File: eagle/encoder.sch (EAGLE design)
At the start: 19 parts, among them IC1 LM339D, J1 SPI, U1 MCP42XXX, U2 ATMEGA328P

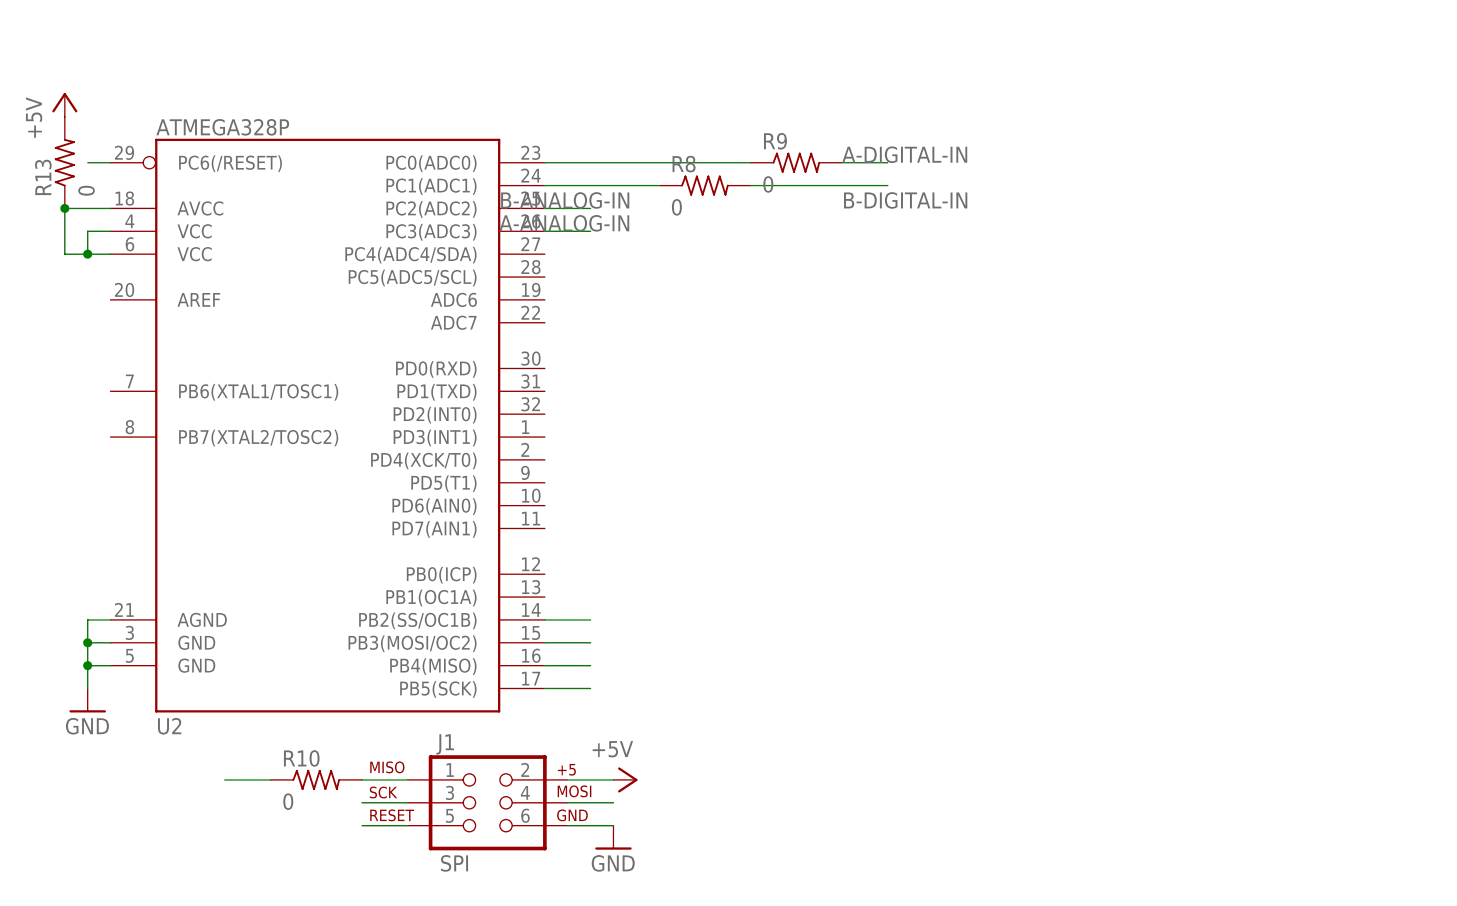
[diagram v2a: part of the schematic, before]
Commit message: Added crystal.
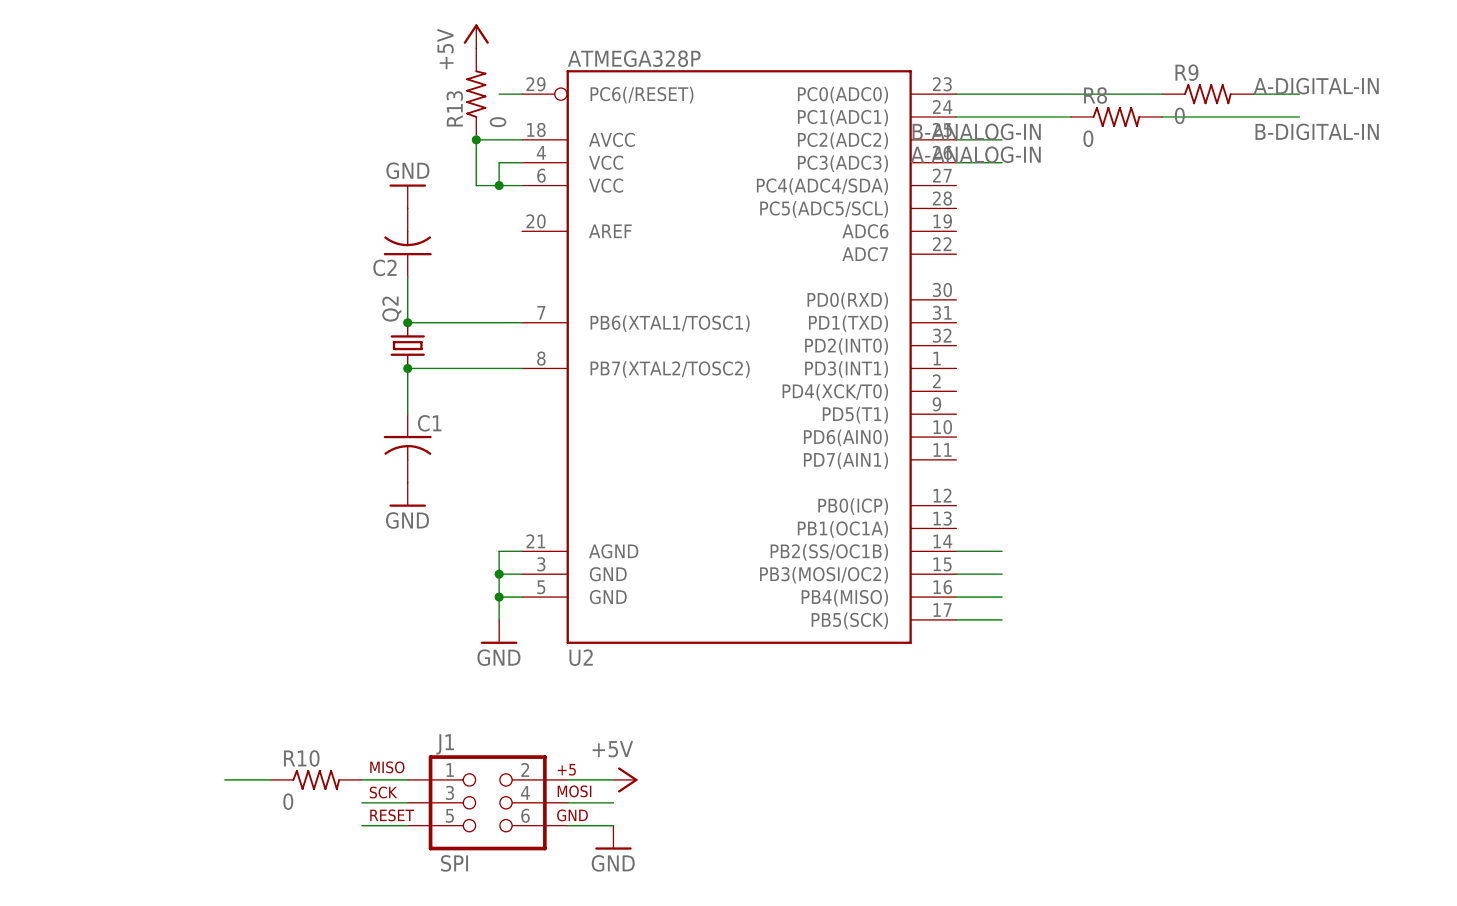
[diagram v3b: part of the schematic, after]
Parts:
- added C1, C2: (no value), resistor:C-USC1206
- added Q2: (no value), crystal:CRYSTALHC49UP
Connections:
- new net N$10: C1.1, Q2.1, U2.PB7(XTAL2/TOSC2)
- new net N$11: C2.1, Q2.2, U2.PB6(XTAL1/TOSC1)
- net GND: now also C1.2, C2.2
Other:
- moved on the sheet: R13, R8, R9, U2
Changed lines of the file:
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@@
 <part name="R13" library="resistor" deviceset="R-US_" device="R1206" value="0"/>
 <part name="P+12" library="supply1" deviceset="+5V" device=""/>
+<part name="Q2" library="crystal" deviceset="CRYSTAL" device="HC49UP"/>
+<part name="C1" library="resistor" deviceset="C-US" device="C1206"/>
+<part name="C2" library="resistor" deviceset="C-US" device="C1206"/>
+<part name="GND9" library="supply1" deviceset="GND" device=""/>
+<part name="GND10" library="supply1" deviceset="GND" device=""/>
 </parts>
 <sheets>
@@
 <instance part="R6" gate="G$1" x="66.04" y="111.76"/>
 <instance part="R7" gate="G$1" x="78.74" y="55.88"/>
-<instance part="U2" gate="G$1" x="25.4" y="177.8"/>
-<instance part="R8" gate="G$1" x="68.58" y="200.66"/>
-<instance part="R9" gate="G$1" x="78.74" y="203.2"/>
+<instance part="U2" gate="G$1" x="71.12" y="185.42"/>
+<instance part="R8" gate="G$1" x="114.3" y="208.28"/>
+<instance part="R9" gate="G$1" x="124.46" y="210.82"/>
 <instance part="R10" gate="G$1" x="25.4" y="134.62"/>
 <instance part="J1" gate="G$1" x="43.18" y="132.08"/>
 <instance part="P+11" gate="1" x="60.96" y="134.62" rot="R270"/>
 <instance part="GND8" gate="1" x="58.42" y="127"/>
-<instance part="GND6" gate="1" x="0" y="142.24"/>
+<instance part="GND6" gate="1" x="45.72" y="149.86"/>
 <instance part="R11" gate="G$1" x="60.96" y="35.56" rot="R90"/>
 <instance part="P+10" gate="1" x="60.96" y="43.18"/>
 <instance part="R12" gate="G$1" x="71.12" y="30.48" rot="R90"/>
-<instance part="R13" gate="G$1" x="-2.54" y="203.2" rot="R90"/>
-<instance part="P+12" gate="1" x="-2.54" y="210.82"/>
+<instance part="R13" gate="G$1" x="43.18" y="210.82" rot="R90"/>
+<instance part="P+12" gate="1" x="43.18" y="218.44"/>
+<instance part="Q2" gate="G$1" x="35.56" y="182.88" rot="R90"/>
+<instance part="C1" gate="G$1" x="35.56" y="172.72"/>
+<instance part="C2" gate="G$1" x="35.56" y="193.04" rot="R180"/>
+<instance part="GND9" gate="1" x="35.56" y="165.1"/>
+<instance part="GND10" gate="1" x="35.56" y="200.66" rot="R180"/>
 </instances>
 <busses>
@@
 <segment>
 <pinref part="U2" gate="G$1" pin="AGND"/>
-<wire x1="2.54" y1="152.4" x2="0" y2="152.4" width="0.1524" layer="91"/>
-<wire x1="0" y1="152.4" x2="0" y2="149.86" width="0.1524" layer="91"/>
+<wire x1="48.26" y1="160.02" x2="45.72" y2="160.02" width="0.1524" layer="91"/>
+<wire x1="45.72" y1="160.02" x2="45.72" y2="157.48" width="0.1524" layer="91"/>
 <pinref part="U2" gate="G$1" pin="GND@1"/>
-<wire x1="0" y1="149.86" x2="0" y2="147.32" width="0.1524" layer="91"/>
-<wire x1="0" y1="147.32" x2="0" y2="144.78" width="0.1524" layer="91"/>
-<wire x1="2.54" y1="149.86" x2="0" y2="149.86" width="0.1524" layer="91"/>
+<wire x1="45.72" y1="157.48" x2="45.72" y2="154.94" width="0.1524" layer="91"/>
+<wire x1="45.72" y1="154.94" x2="45.72" y2="152.4" width="0.1524" layer="91"/>
+<wire x1="48.26" y1="157.48" x2="45.72" y2="157.48" width="0.1524" layer="91"/>
 <pinref part="U2" gate="G$1" pin="GND@2"/>
-<wire x1="2.54" y1="147.32" x2="0" y2="147.32" width="0.1524" layer="91"/>
+<wire x1="48.26" y1="154.94" x2="45.72" y2="154.94" width="0.1524" layer="91"/>
 <pinref part="GND6" gate="1" pin="GND"/>
-<junction x="0" y="149.86"/>
-<junction x="0" y="147.32"/>
+<junction x="45.72" y="157.48"/>
+<junction x="45.72" y="154.94"/>
+</segment>
+<segment>
+<pinref part="C1" gate="G$1" pin="2"/>
+<pinref part="GND9" gate="1" pin="GND"/>
+</segment>
+<segment>
+<pinref part="C2" gate="G$1" pin="2"/>
+<pinref part="GND10" gate="1" pin="GND"/>
 </segment>
 </net>
@@
 <segment>
 <pinref part="U2" gate="G$1" pin="PC3(ADC3)"/>
-<wire x1="50.8" y1="195.58" x2="55.88" y2="195.58" width="0.1524" layer="91"/>
-<label x="45.72" y="195.58" size="1.778" layer="95"/>
+<wire x1="96.52" y1="203.2" x2="101.6" y2="203.2" width="0.1524" layer="91"/>
+<label x="91.44" y="203.2" size="1.778" layer="95"/>
 </segment>
 <segment>
@@
 <segment>
 <pinref part="U2" gate="G$1" pin="PC2(ADC2)"/>
-<wire x1="50.8" y1="198.12" x2="55.88" y2="198.12" width="0.1524" layer="91"/>
-<label x="45.72" y="198.12" size="1.778" layer="95"/>
+<wire x1="96.52" y1="205.74" x2="101.6" y2="205.74" width="0.1524" layer="91"/>
+<label x="91.44" y="205.74" size="1.778" layer="95"/>
 </segment>
 <segment>
@@
 <pinref part="U2" gate="G$1" pin="PC1(ADC1)"/>
 <pinref part="R8" gate="G$1" pin="1"/>
-<wire x1="63.5" y1="200.66" x2="50.8" y2="200.66" width="0.1524" layer="91"/>
+<wire x1="109.22" y1="208.28" x2="96.52" y2="208.28" width="0.1524" layer="91"/>
 </segment>
 </net>
@@
 <pinref part="U2" gate="G$1" pin="PC0(ADC0)"/>
 <pinref part="R9" gate="G$1" pin="1"/>
-<wire x1="73.66" y1="203.2" x2="50.8" y2="203.2" width="0.1524" layer="91"/>
+<wire x1="119.38" y1="210.82" x2="96.52" y2="210.82" width="0.1524" layer="91"/>
 </segment>
 </net>
@@
 <segment>
 <pinref part="R9" gate="G$1" pin="2"/>
-<wire x1="83.82" y1="203.2" x2="88.9" y2="203.2" width="0.1524" layer="91"/>
-<label x="83.82" y="203.2" size="1.778" layer="95"/>
+<wire x1="129.54" y1="210.82" x2="134.62" y2="210.82" width="0.1524" layer="91"/>
+<label x="129.54" y="210.82" size="1.778" layer="95"/>
 </segment>
 <segment>
@@
 <segment>
 <pinref part="R8" gate="G$1" pin="2"/>
-<wire x1="73.66" y1="200.66" x2="88.9" y2="200.66" width="0.1524" layer="91"/>
-<label x="83.82" y="198.12" size="1.778" layer="95"/>
+<wire x1="119.38" y1="208.28" x2="134.62" y2="208.28" width="0.1524" layer="91"/>
+<label x="129.54" y="205.74" size="1.778" layer="95"/>
 </segment>
 <segment>
@@
 <segment>
 <pinref part="U2" gate="G$1" pin="PB3(MOSI/OC2)"/>
-<wire x1="50.8" y1="149.86" x2="55.88" y2="149.86" width="0.1524" layer="91"/>
+<wire x1="96.52" y1="157.48" x2="101.6" y2="157.48" width="0.1524" layer="91"/>
 </segment>
 <segment>
@@
 <segment>
 <pinref part="U2" gate="G$1" pin="PB4(MISO)"/>
-<wire x1="50.8" y1="147.32" x2="55.88" y2="147.32" width="0.1524" layer="91"/>
+<wire x1="96.52" y1="154.94" x2="101.6" y2="154.94" width="0.1524" layer="91"/>
 </segment>
 <segment>
@@
 <segment>
 <pinref part="U2" gate="G$1" pin="PB5(SCK)"/>
-<wire x1="50.8" y1="144.78" x2="55.88" y2="144.78" width="0.1524" layer="91"/>
+<wire x1="96.52" y1="152.4" x2="101.6" y2="152.4" width="0.1524" layer="91"/>
 </segment>
 <segment>
@@
 <segment>
 <pinref part="U2" gate="G$1" pin="PC6(/RESET)"/>
-<wire x1="2.54" y1="203.2" x2="0" y2="203.2" width="0.1524" layer="91"/>
+<wire x1="48.26" y1="210.82" x2="45.72" y2="210.82" width="0.1524" layer="91"/>
 </segment>
 <segment>
@@
 <segment>
 <pinref part="U2" gate="G$1" pin="PB2(SS/OC1B)"/>
-<wire x1="50.8" y1="152.4" x2="55.88" y2="152.4" width="0.1524" layer="91"/>
+<wire x1="96.52" y1="160.02" x2="101.6" y2="160.02" width="0.1524" layer="91"/>
 </segment>
 </net>
@@
 <segment>
 <pinref part="U2" gate="G$1" pin="VCC@2"/>
-<wire x1="2.54" y1="193.04" x2="0" y2="193.04" width="0.1524" layer="91"/>
-<wire x1="0" y1="193.04" x2="0" y2="195.58" width="0.1524" layer="91"/>
+<wire x1="48.26" y1="200.66" x2="45.72" y2="200.66" width="0.1524" layer="91"/>
+<wire x1="45.72" y1="200.66" x2="45.72" y2="203.2" width="0.1524" layer="91"/>
 <pinref part="U2" gate="G$1" pin="VCC@1"/>
-<wire x1="2.54" y1="195.58" x2="0" y2="195.58" width="0.1524" layer="91"/>
-<wire x1="0" y1="193.04" x2="-2.54" y2="193.04" width="0.1524" layer="91"/>
+<wire x1="48.26" y1="203.2" x2="45.72" y2="203.2" width="0.1524" layer="91"/>
+<wire x1="45.72" y1="200.66" x2="43.18" y2="200.66" width="0.1524" layer="91"/>
 <pinref part="U2" gate="G$1" pin="AVCC"/>
-<wire x1="-2.54" y1="198.12" x2="2.54" y2="198.12" width="0.1524" layer="91"/>
+<wire x1="43.18" y1="205.74" x2="48.26" y2="205.74" width="0.1524" layer="91"/>
 <pinref part="R13" gate="G$1" pin="1"/>
-<wire x1="-2.54" y1="193.04" x2="-2.54" y2="198.12" width="0.1524" layer="91"/>
-<junction x="-2.54" y="198.12"/>
-<junction x="0" y="193.04"/>
-</segment>
-</net>
+<wire x1="43.18" y1="200.66" x2="43.18" y2="205.74" width="0.1524" layer="91"/>
+<junction x="43.18" y="205.74"/>
+<junction x="45.72" y="200.66"/>
+</segment>
+</net>
+<net name="N$10" class="0">
+<segment>
+<pinref part="U2" gate="G$1" pin="PB7(XTAL2/TOSC2)"/>
+<pinref part="Q2" gate="G$1" pin="1"/>
+<wire x1="48.26" y1="180.34" x2="35.56" y2="180.34" width="0.1524" layer="91"/>
+<pinref part="C1" gate="G$1" pin="1"/>
+<wire x1="35.56" y1="175.26" x2="35.56" y2="180.34" width="0.1524" layer="91"/>
+<junction x="35.56" y="180.34"/>
+</segment>
+</net>
+<net name="N$11" class="0">
+<segment>
+<pinref part="U2" gate="G$1" pin="PB6(XTAL1/TOSC1)"/>
+<pinref part="Q2" gate="G$1" pin="2"/>
+<wire x1="48.26" y1="185.42" x2="35.56" y2="185.42" width="0.1524" layer="91"/>
+<pinref part="C2" gate="G$1" pin="1"/>
+<wire x1="35.56" y1="190.5" x2="35.56" y2="185.42" width="0.1524" layer="91"/>
+<junction x="35.56" y="185.42"/>
+</segment>
+</net>
